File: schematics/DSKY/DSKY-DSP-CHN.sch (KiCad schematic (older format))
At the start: 5 parts, among them U20 74LS273, U21 74LS273, U22 74LS273, U5 74LS04, U7 74LS08

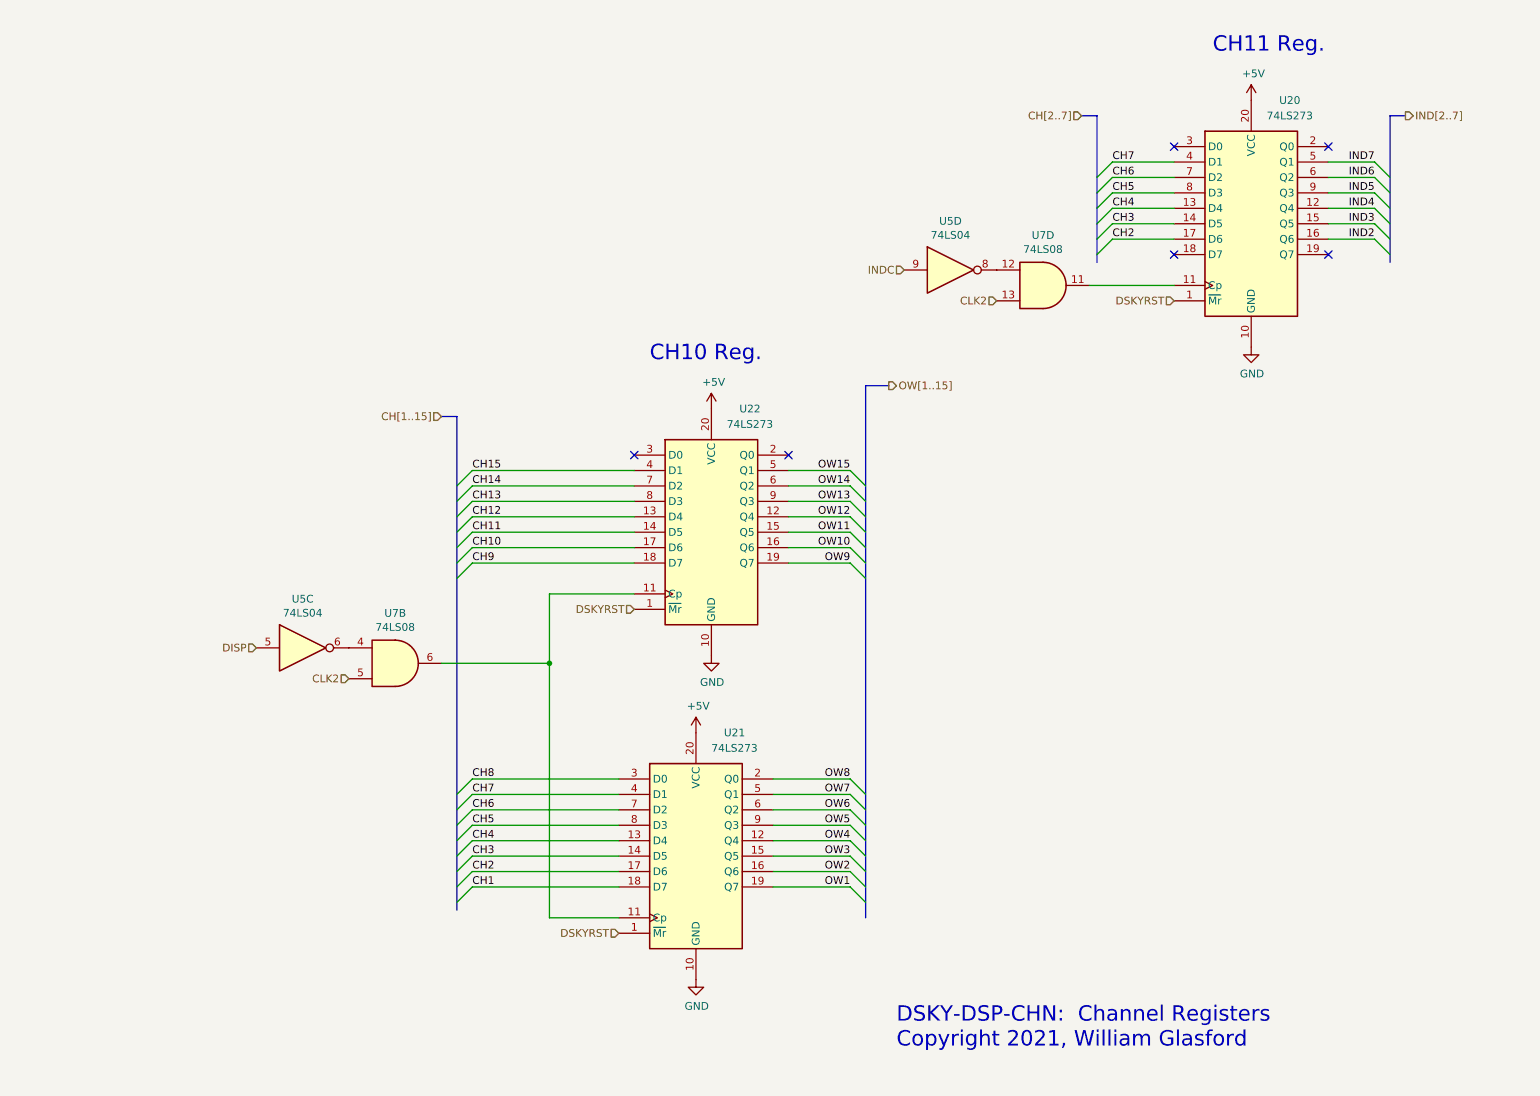
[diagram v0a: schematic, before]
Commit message: Using 4 LED driver chips.
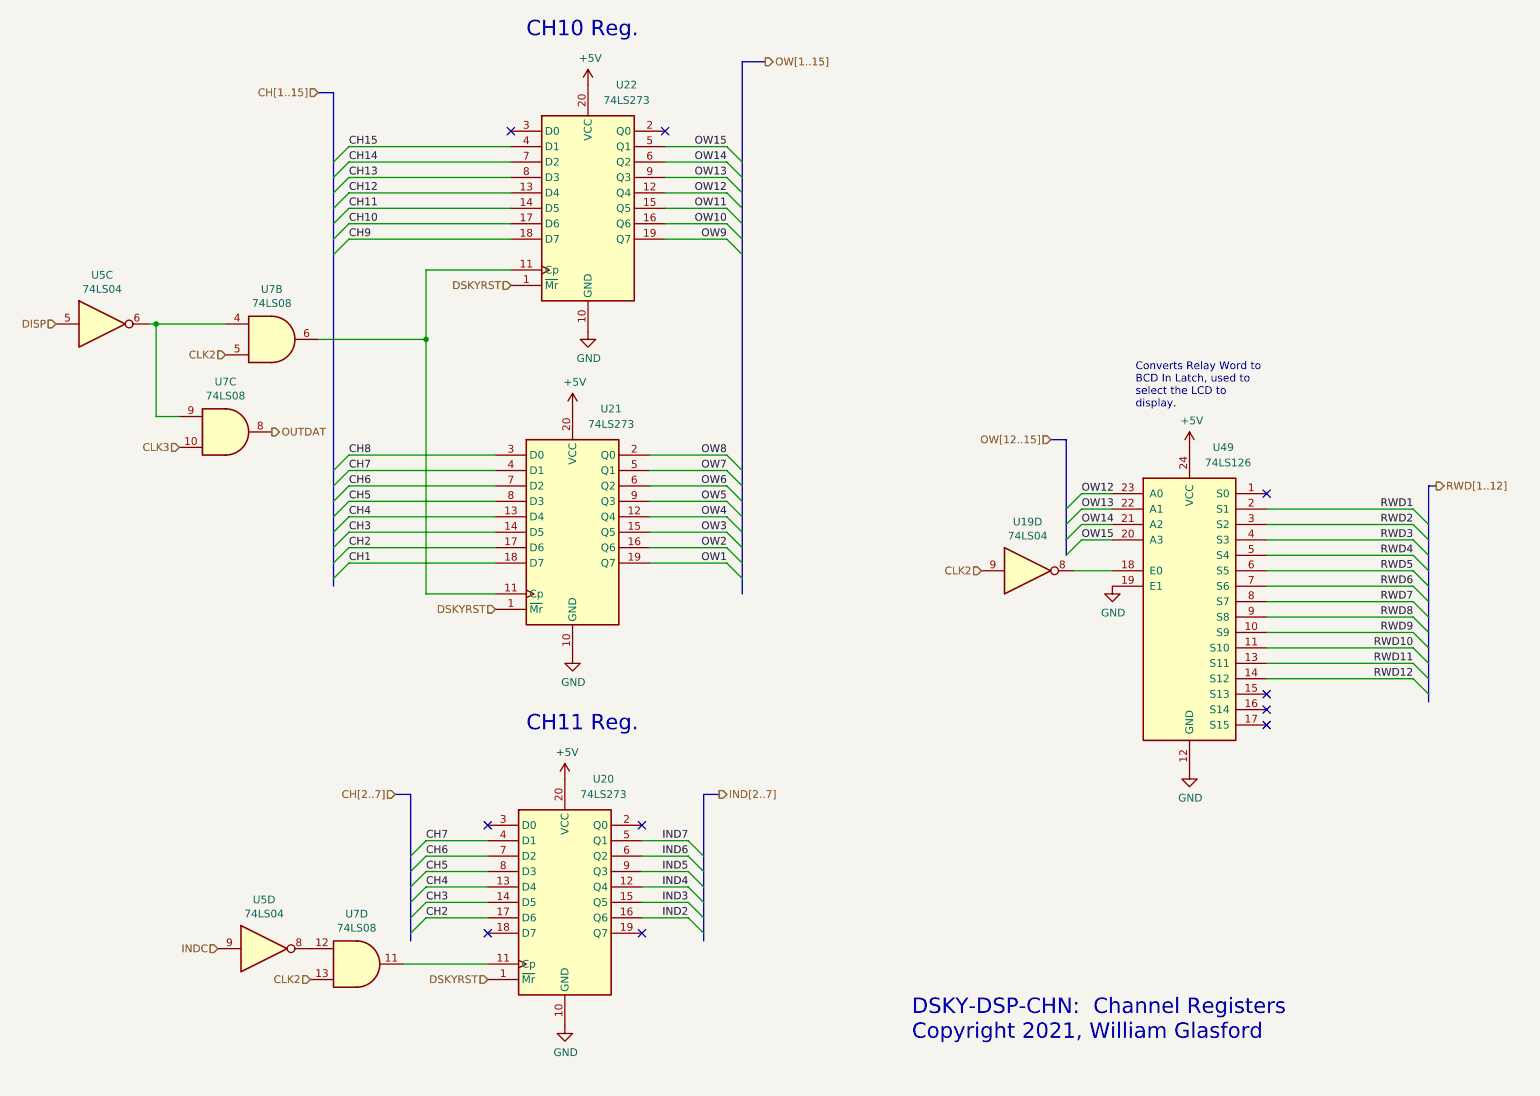
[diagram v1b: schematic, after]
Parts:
- added U19: 74LS04, symbol 74xx:74LS04
- added U49: 74LS126, symbol 74xx:74LS154
- added unit 3 of U7
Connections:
- net +5V: now also U49.24 (VCC)
- net CLK2: now also U19.9
- net GND: now also U49.12 (GND), U49.19 (E1)
- net OW12: now also U49.23 (A0)
- net OW13: now also U49.22 (A1)
- net OW14: now also U49.21 (A2)
- net OW15: now also U49.20 (A3)
- net at U5.6, U7.4: now also U7.9
- new net: U19.8, U49.18 (E0)
- new net CLK3: U7.10
- new net OUTDAT: U7.8
- new net RWD1: U49.2 (S1)
- new net RWD10: U49.11 (S10)
- new net RWD11: U49.13 (S11)
- new net RWD12: U49.14 (S12)
- new net RWD2: U49.3 (S2)
- new net RWD3: U49.4 (S3)
- new net RWD4: U49.5 (S4)
- new net RWD5: U49.6 (S5)
- new net RWD6: U49.7 (S6)
- new net RWD7: U49.8 (S7)
- new net RWD8: U49.9 (S8)
- new net RWD9: U49.10 (S9)
- no-connect marks 6 -> 10
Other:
- note added: "Converts Relay Word to\nBCD In Latch, used to\nselect the LCD to \ndisplay."
- moved on the sheet: U20, U21, U22, U5C, U5D, U7B, U7D

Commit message: Modified to use fourth display decoder chip.
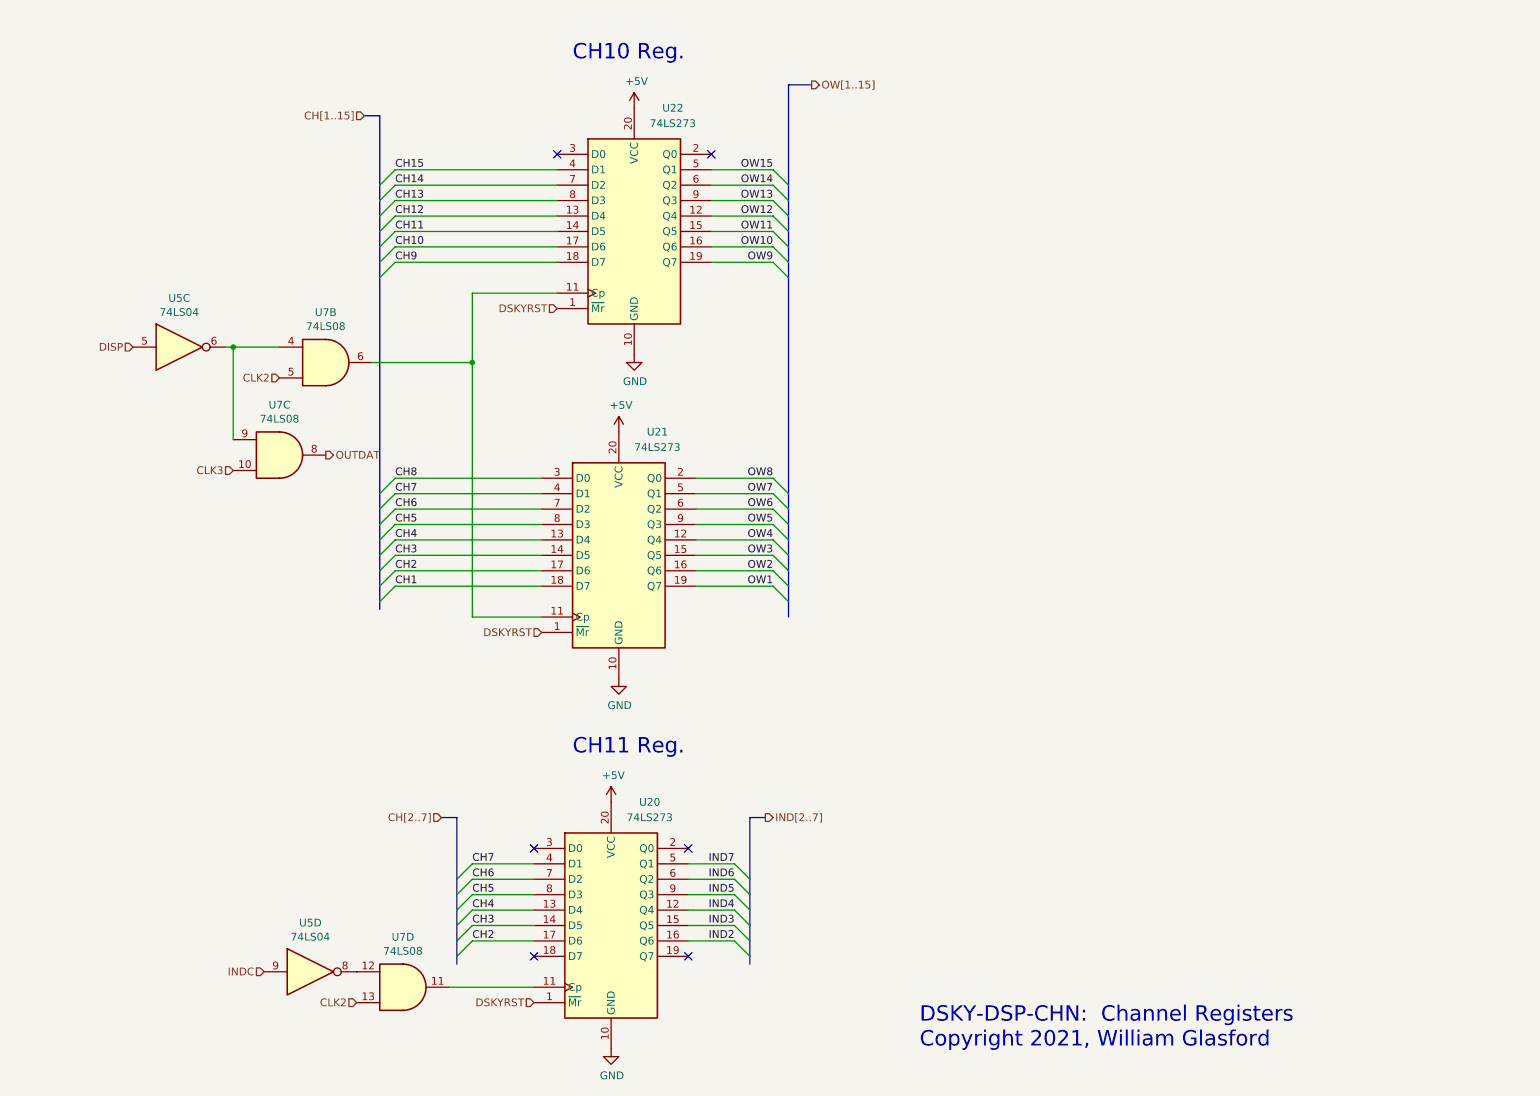
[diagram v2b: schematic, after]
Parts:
- removed U19: 74LS04, symbol 74xx:74LS04
- removed U49: 74LS126, symbol 74xx:74LS154
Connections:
- no-connect marks 10 -> 6
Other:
- note removed: "Converts Relay Word to\nBCD In Latch, used to\nselect the LCD to \ndisplay."
- moved on the sheet: U20, U21, U22, U5C, U5D, U7B, U7C, U7D
